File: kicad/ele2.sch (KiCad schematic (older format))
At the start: 3 parts, among them SW1 SW_Push, U1 WeMos_D1_mini, U2 HX711_module

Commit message: Copy d1 mini symbol to local library
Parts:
- U1: symbol MCU_Module:WeMos_D1_mini -> ele2:WeMos_D1_mini
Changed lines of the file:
@@
 $EndDescr
 $Comp
-L MCU_Module:WeMos_D1_mini U1
+L ele2:WeMos_D1_mini U1
 U 1 1 5E80C742
 P 4250 3950
@@
 Text GLabel 7300 3950 2    50   Input ~ 0
 LOAD_CELLS
-Wire Bus Line
-	7200 3950 7200 4600
 Text Notes 7050 4900 0    50   ~ 0
 *)
 Text Notes 6550 5750 0    50   ~ 0
 *) E- manually connected to GND\n  due to missing trace on board
+Wire Bus Line
+	7200 3950 7200 4600
 $EndSCHEMATC

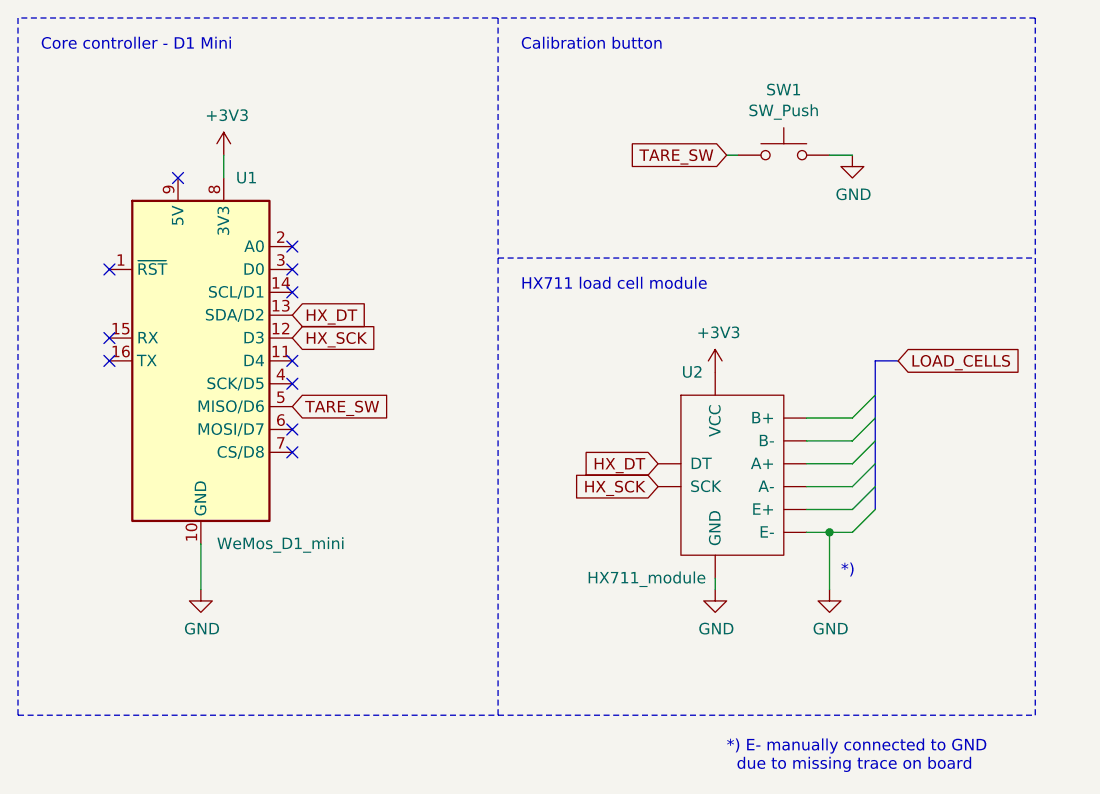
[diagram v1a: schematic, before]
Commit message: Model in load cells in subsheet
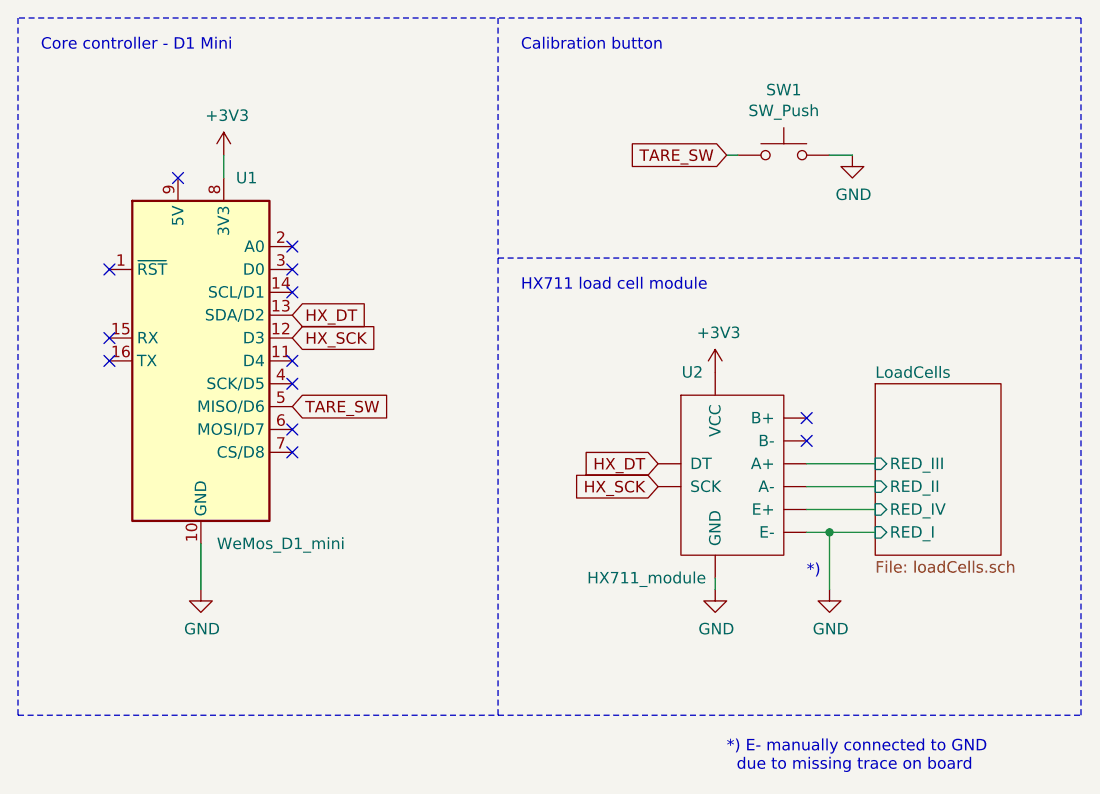
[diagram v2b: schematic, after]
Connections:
- net LoadCells/RED_IV: now reaches U2.~ (VCC)
- new net LoadCells/RED_II: U2.~ (VCC)
- new net LoadCells/RED_III: U2.~ (VCC)
- no-connect marks 11 -> 13
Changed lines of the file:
@@
 $Descr A4 11693 8268
 encoding utf-8
-Sheet 1 1
+Sheet 1 2
 Title "coffee-sensor"
 Date "2020-03-29"
@@
 NoConn ~ 4650 4250
 NoConn ~ 4650 4350
-Wire Bus Line
-	7200 3950 7300 3950
 Text GLabel 4650 3750 2    50   Input ~ 0
 HX_DT
@@
 	3450 2450 3450 5500
 Wire Notes Line
-	3450 5500 7900 5500
+	3450 5500 8100 5500
 Wire Notes Line
-	7900 5500 7900 2450
+	8100 5500 8100 2450
 Wire Notes Line
-	7900 2450 3450 2450
+	8100 2450 3450 2450
 Wire Notes Line
 	5550 2450 5550 5500
 Wire Notes Line
-	5550 3500 7900 3500
+	5550 3500 8100 3500
 Text Notes 5650 2600 0    50   ~ 0
 Calibration button
@@
 Text Notes 3550 2600 0    50   ~ 0
 Core controller - D1 Mini
-Entry Wire Line
-	7200 4600 7100 4700
-Entry Wire Line
-	7200 4500 7100 4600
-Entry Wire Line
-	7200 4400 7100 4500
-Entry Wire Line
-	7200 4300 7100 4400
-Entry Wire Line
-	7200 4200 7100 4300
-Entry Wire Line
-	7200 4100 7100 4200
-Wire Wire Line
-	6900 4200 7100 4200
-Wire Wire Line
-	6900 4300 7100 4300
-Wire Wire Line
-	6900 4400 7100 4400
-Wire Wire Line
-	6900 4500 7100 4500
-Wire Wire Line
-	6900 4600 7100 4600
 Wire Wire Line
 	6900 4700 7000 4700
 Connection ~ 7000 4700
-Wire Wire Line
-	7000 4700 7100 4700
 $Comp
 L power:GND #PWR?
@@
 Wire Wire Line
 	7000 4700 7000 4950
-Text GLabel 7300 3950 2    50   Input ~ 0
-LOAD_CELLS
-Text Notes 7050 4900 0    50   ~ 0
+Text Notes 6900 4900 0    50   ~ 0
 *)
 Text Notes 6550 5750 0    50   ~ 0
 *) E- manually connected to GND\n  due to missing trace on board
-Wire Bus Line
-	7200 3950 7200 4600
+$Sheet
+S 7200 4050 550  750
+U 5E83A8FB
+F0 "LoadCells" 50
+F1 "loadCells.sch" 50
+F2 "RED_II" I L 7200 4500 50
+F3 "RED_I" I L 7200 4700 50
+F4 "RED_IV" I L 7200 4600 50
+F5 "RED_III" I L 7200 4400 50
+$EndSheet
+NoConn ~ 6900 4200
+NoConn ~ 6900 4300
+Wire Wire Line
+	6900 4400 7200 4400
+Wire Wire Line
+	6900 4500 7200 4500
+Wire Wire Line
+	6900 4600 7200 4600
+Wire Wire Line
+	7000 4700 7200 4700
 $EndSCHEMATC

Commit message: Update schematic
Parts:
- removed SW1: SW_Push, symbol Switch:SW_Push
- added U?: Adafruit_SSD1306, symbol ele2:Adafruit_SSD1306
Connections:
- net +3V3: now also U?.~ (SDA)
- net GND: now also U?.~ (SDA)
- net HX_DT: now also U1.14 (SCL/D1); no longer U1.13 (SDA/D2)
- net HX_SCK: now also U1.13 (SDA/D2); no longer U1.12 (D3)
- net SCREEN_SCL: now reaches U1.4 (SCK/D5)
- net SCREEN_SCL: now also U?.~ (SDA)
- net TARE_SW renamed SCREEN_SDA
- net SCREEN_SDA: now also U?.~ (SDA)
- no-connect marks 13 -> 12
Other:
- note added: "OLED display"
- note removed: "Calibration button"
- moved on the sheet: U2
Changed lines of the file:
@@
 	4250 4950 4250 4750
-$Comp
-L Switch:SW_Push SW1
-U 1 1 5E80F0CB
-P 6800 3050
-F 0 "SW1" H 6800 3335 50  0000 C CNN
-F 1 "SW_Push" H 6800 3244 50  0000 C CNN
-F 2 "" H 6800 3250 50  0001 C CNN
-F 3 "~" H 6800 3250 50  0001 C CNN
-	1    6800 3050
-	1    0    0    -1
-$EndComp
-$Comp
-L power:GND #PWR?
-U 1 1 5E81082F
-P 7100 3050
-F 0 "#PWR?" H 7100 2800 50  0001 C CNN
-F 1 "GND" H 7105 2877 50  0000 C CNN
-F 2 "" H 7100 3050 50  0001 C CNN
-F 3 "" H 7100 3050 50  0001 C CNN
-	1    7100 3050
-	1    0    0    -1
-$EndComp
-Wire Wire Line
-	6550 3050 6600 3050
-Wire Wire Line
-	7000 3050 7100 3050
 $Comp
 L ele2:HX711_module U2
 U 1 1 5E815E00
-P 6550 4450
-F 0 "U2" H 6400 4900 50  0000 C CNN
-F 1 "HX711_module" H 6200 4000 50  0000 C CNN
-F 2 "" H 6550 4450 50  0001 C CNN
-F 3 "" H 6550 4450 50  0001 C CNN
-	1    6550 4450
-	1    0    0    -1
-$EndComp
-$Comp
-L power:+3V3 #PWR?
-U 1 1 5E81AC21
-P 6500 4000
-F 0 "#PWR?" H 6500 3850 50  0001 C CNN
-F 1 "+3V3" H 6515 4173 50  0000 C CNN
-F 2 "" H 6500 4000 50  0001 C CNN
-F 3 "" H 6500 4000 50  0001 C CNN
-	1    6500 4000
+P 6550 4700
+F 0 "U2" H 6400 5150 50  0000 C CNN
+F 1 "HX711_module" H 6200 4250 50  0000 C CNN
+F 2 "" H 6550 4700 50  0001 C CNN
+F 3 "" H 6550 4700 50  0001 C CNN
+	1    6550 4700
 	1    0    0    -1
 $EndComp
@@
 L power:GND #PWR?
 U 1 1 5E81C444
-P 6500 4950
-F 0 "#PWR?" H 6500 4700 50  0001 C CNN
-F 1 "GND" H 6505 4777 50  0000 C CNN
-F 2 "" H 6500 4950 50  0001 C CNN
-F 3 "" H 6500 4950 50  0001 C CNN
-	1    6500 4950
+P 6500 5200
+F 0 "#PWR?" H 6500 4950 50  0001 C CNN
+F 1 "GND" H 6505 5027 50  0000 C CNN
+F 2 "" H 6500 5200 50  0001 C CNN
+F 3 "" H 6500 5200 50  0001 C CNN
+	1    6500 5200
 	1    0    0    -1
 $EndComp
 Wire Wire Line
-	6500 4900 6500 4950
+	6500 5150 6500 5200
 NoConn ~ 4650 3450
 NoConn ~ 4650 3550
-NoConn ~ 4650 3650
-NoConn ~ 4650 4050
 NoConn ~ 4650 3950
-Text GLabel 6550 3050 0    50   Input ~ 0
-TARE_SW
-Text GLabel 4650 4150 2    50   Input ~ 0
-TARE_SW
+Text GLabel 4650 4050 2    50   Input ~ 0
+SCREEN_SCL
 NoConn ~ 4650 4250
 NoConn ~ 4650 4350
+Text GLabel 4650 3650 2    50   Input ~ 0
+HX_DT
+Text GLabel 6250 4750 0    50   Input ~ 0
+HX_SCK
 Text GLabel 4650 3750 2    50   Input ~ 0
-HX_DT
-Text GLabel 6250 4500 0    50   Input ~ 0
 HX_SCK
-Text GLabel 4650 3850 2    50   Input ~ 0
-HX_SCK
-Text GLabel 6250 4400 0    50   Input ~ 0
+Text GLabel 6250 4650 0    50   Input ~ 0
 HX_DT
 Wire Notes Line
@@
 	5550 2450 5550 5500
 Wire Notes Line
-	5550 3500 8100 3500
-Text Notes 5650 2600 0    50   ~ 0
-Calibration button
-Text Notes 5650 3650 0    50   ~ 0
+	5550 3750 8100 3750
+Text Notes 5650 3900 0    50   ~ 0
 HX711 load cell module
 Text Notes 3550 2600 0    50   ~ 0
 Core controller - D1 Mini
 Wire Wire Line
-	6900 4700 7000 4700
-Connection ~ 7000 4700
+	6900 4950 7000 4950
+Connection ~ 7000 4950
 $Comp
 L power:GND #PWR?
 U 1 1 5E83F78A
-P 7000 4950
-F 0 "#PWR?" H 7000 4700 50  0001 C CNN
-F 1 "GND" H 7005 4777 50  0000 C CNN
-F 2 "" H 7000 4950 50  0001 C CNN
-F 3 "" H 7000 4950 50  0001 C CNN
-	1    7000 4950
+P 7000 5200
+F 0 "#PWR?" H 7000 4950 50  0001 C CNN
+F 1 "GND" H 7005 5027 50  0000 C CNN
+F 2 "" H 7000 5200 50  0001 C CNN
+F 3 "" H 7000 5200 50  0001 C CNN
+	1    7000 5200
 	1    0    0    -1
 $EndComp
 Wire Wire Line
-	7000 4700 7000 4950
-Text Notes 6900 4900 0    50   ~ 0
+	7000 4950 7000 5200
+Text Notes 6900 5150 0    50   ~ 0
 *)
 Text Notes 6550 5750 0    50   ~ 0
 *) E- manually connected to GND\n  due to missing trace on board
 $Sheet
-S 7200 4050 550  750
+S 7200 4300 550  750
 U 5E83A8FB
 F0 "LoadCells" 50
 F1 "loadCells.sch" 50
-F2 "RED_II" I L 7200 4500 50
-F3 "RED_I" I L 7200 4700 50
-F4 "RED_IV" I L 7200 4600 50
-F5 "RED_III" I L 7200 4400 50
+F2 "RED_II" I L 7200 4750 50
+F3 "RED_I" I L 7200 4950 50
+F4 "RED_IV" I L 7200 4850 50
+F5 "RED_III" I L 7200 4650 50
 $EndSheet
-NoConn ~ 6900 4200
-NoConn ~ 6900 4300
+NoConn ~ 6900 4450
+NoConn ~ 6900 4550
 Wire Wire Line
-	6900 4400 7200 4400
+	6900 4650 7200 4650
 Wire Wire Line
-	6900 4500 7200 4500
+	6900 4750 7200 4750
 Wire Wire Line
-	6900 4600 7200 4600
+	6900 4850 7200 4850
 Wire Wire Line
-	7000 4700 7200 4700
+	7000 4950 7200 4950
+NoConn ~ 4650 3850
+Text GLabel 4650 4150 2    50   Input ~ 0
+SCREEN_SDA
+$Comp
+L ele2:Adafruit_SSD1306 U?
+U 1 1 5EBEA0D0
+P 6750 3100
+F 0 "U?" H 7228 3146 50  0000 L CNN
+F 1 "Adafruit_SSD1306" H 7228 3055 50  0000 L CNN
+F 2 "" H 6750 3050 50  0001 C CNN
+F 3 "" H 6750 3050 50  0001 C CNN
+	1    6750 3100
+	1    0    0    -1
+$EndComp
+$Comp
+L power:+3V3 #PWR?
+U 1 1 5E81AC21
+P 6500 4250
+F 0 "#PWR?" H 6500 4100 50  0001 C CNN
+F 1 "+3V3" H 6515 4423 50  0000 C CNN
+F 2 "" H 6500 4250 50  0001 C CNN
+F 3 "" H 6500 4250 50  0001 C CNN
+	1    6500 4250
+	1    0    0    -1
+$EndComp
+$Comp
+L power:+3V3 #PWR?
+U 1 1 5EBEDF9F
+P 6850 2700
+F 0 "#PWR?" H 6850 2550 50  0001 C CNN
+F 1 "+3V3" H 6865 2873 50  0000 C CNN
+F 2 "" H 6850 2700 50  0001 C CNN
+F 3 "" H 6850 2700 50  0001 C CNN
+	1    6850 2700
+	1    0    0    -1
+$EndComp
+$Comp
+L power:GND #PWR?
+U 1 1 5EBEE845
+P 6850 3500
+F 0 "#PWR?" H 6850 3250 50  0001 C CNN
+F 1 "GND" H 6855 3327 50  0000 C CNN
+F 2 "" H 6850 3500 50  0001 C CNN
+F 3 "" H 6850 3500 50  0001 C CNN
+	1    6850 3500
+	1    0    0    -1
+$EndComp
+Text GLabel 6400 3150 0    50   Input ~ 0
+SCREEN_SCL
+Text GLabel 6400 3050 0    50   Input ~ 0
+SCREEN_SDA
+Text Notes 5650 2600 0    50   ~ 0
+OLED display
 $EndSCHEMATC
